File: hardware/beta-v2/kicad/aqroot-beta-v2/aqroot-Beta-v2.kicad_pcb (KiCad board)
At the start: 6 copper layers, 72 x 148 mm, 324 parts, among them J1 FH69-50S-0.5SH, J2 Molex_5025700893, J3 USB_C_Receptacle_USB2.0_16P, J4 JST-PH-2 BATTERY, J5 COMMUNITY_PORT_1x24, J6 JST-PH-2 SPEAKER, J7 BM02B-ACHSS-GAN-ETF, J8 QWIIC_STEMMA_QT, Q1 AO3400A, Q10 2N7002, Q2 NTMD4820N, Q3 NTMD4820N, Q4 BSS138, Q5 AO3401A, Q6 BSS138, Q7 BSS138, Q8 BSS138, Q9 BSS138, SW1 BOOT, SW2 UP, SW3 DOWN, SW4 LEFT, SW5 RIGHT, SW6 A_SELECT, SW7 B_BACK, SW9 SW_SPDT, U1 ESP32-S3-WROOM-1, U10 USBLC6-2SC6, U11 BQ25185, U12 TPS63020, U13 TPS61023, U14 MAX17048, U16 TCA4307DGKR, U17 TPS61169DCKR, U18 LTC4368-1, U19 TLV7032, U2 PCAL9535APW, U20 TPS22950C, U21 TPS61023, U22 TPS22950C, U23 PCAL9535APW, U3 PCAL9535APW, U4 BMI270, U5 MAX98357A, U6 TSOP38238, U7 E07-400M10S, U8 E22-900M22S, U9 ST25R3916-AQET, Y1 27.12MHz 10pF 3225-4P

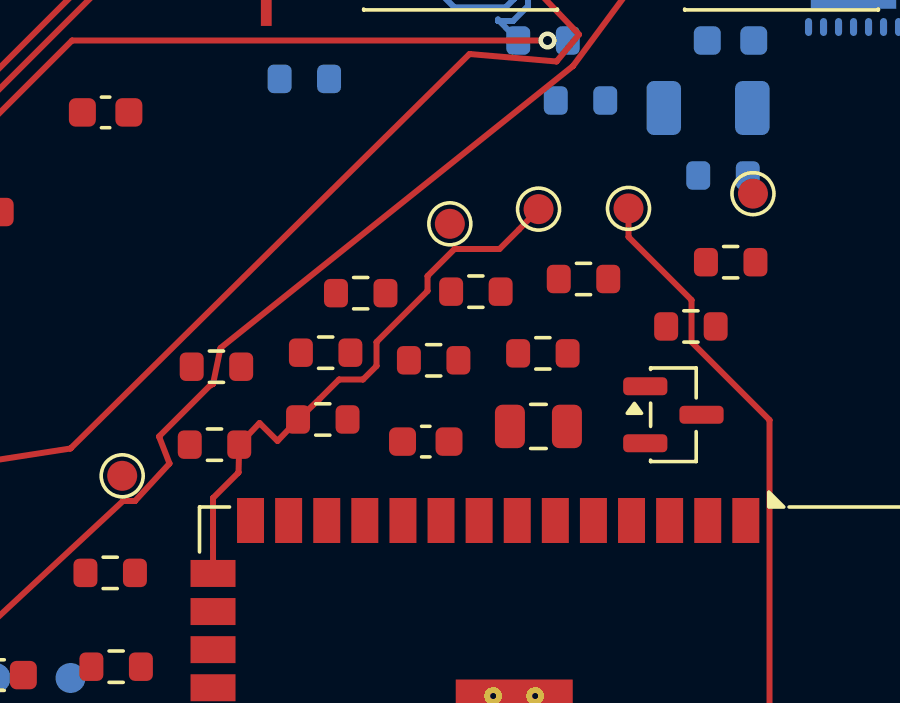
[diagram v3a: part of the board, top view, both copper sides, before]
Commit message: FBV2-P2-022: D-320 FIFTEENTH REST-OF-BOARD INCREMENTAL INCREMENT ROUTED + PROMOTED — the IR transmit carrier CONTROL leg IR_TX_GPIO16 (U1.9 ESP32 GPIO16 -> R22.1 series-drive resistor), a dedicated 2-pad point-to-point net, SAME-LAYER F.Cu MST with NO via (the cleanest class), a clean increment in an OPEN region 35.2 mm clear of BAT_PROTECTED_P (zero D-269 involvement); the low-current MCU control GPIO isolated by series R22 from the IR_GATE switch node + IR_LED_A/K emitter power (both excluded switching/emitter nets); a governed CTO ACCEPT + PROMOTE, ZERO router-logic change
Screen w/screen_020.py (142 unrouted rest nets, 42 ALLOW/100 EXCL; auto-classifier
converter-switching/USB-C traps rejected on role) + geometry vet w/vet_021.py verified
the isolation (/IR_TX_GPIO16 = {U1.9,R22.1}; R22.2 belongs to the separate IR_GATE net;
emitter power is IR_LED_A/K) and selected IR_TX_GPIO16 over Net-(U1-EN)/RESERVED_SPARE on
merit. GROUPS['IR_TX_GPIO16'] entry only; route ALL OK (13 F.Cu seg, 0 via, legal
same-layer detour around the GND pinch); gate PASS every check; promote.

sha 57dcc8af.. -> 4e706490389655cb8b68f8c15249a813072f36a9ea9e6ffaeb1fdd2194c0bf34;
tracks 716->729 (+13 F.Cu 0.200mm); vias 67 (unchanged); ratsnest 672->671; journal
109->110. New G32 + incremental_probe_020.py; router_regression ALL PASS G1-G32 twice;
probes _006..020 + phaseB PASS; live_fingerprint bumped; independent kicad-cli DRC
clearance 0; D-269/D-264/DRU board-swap A/B pre-existing/intrinsic flakes (not
regressions). 141/164 rest nets unrouted. Rollback: pre-D-320 sha 57dcc8af.. (committed
D-319, parent 8d27e3a).

Co-Authored-By: Claude Opus 4.8 (1M context) <noreply@anthropic.com>
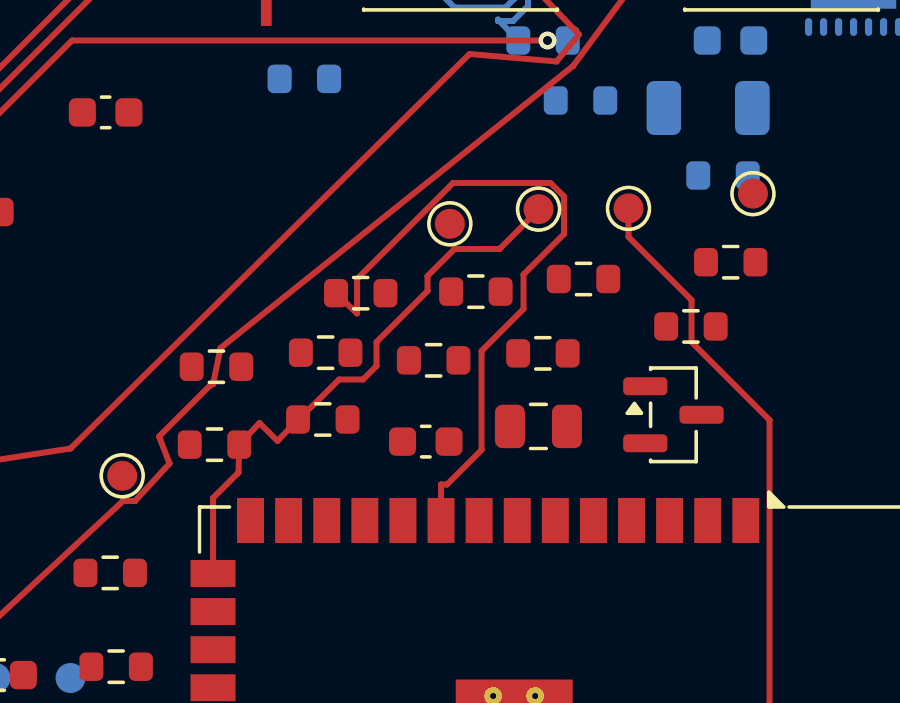
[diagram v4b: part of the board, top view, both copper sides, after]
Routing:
- net /IR_TX_GPIO16: track 0.00 -> 23.2 mm
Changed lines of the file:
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@@
+	)
+	(segment
+		(start 54.2 113.6)
+		(end 54.2 116.9)
+		(width 0.2)
+		(layer "F.Cu")
+		(net "/IR_TX_GPIO16")
+	)
+	(segment
+		(start 55.6 112.2)
+		(end 54.2 113.6)
+		(width 0.2)
+		(layer "F.Cu")
+		(net "/IR_TX_GPIO16")
+	)
+	(segment
+		(start 50.05 111.2)
+		(end 53.25 108)
+		(width 0.2)
+		(layer "F.Cu")
+		(net "/IR_TX_GPIO16")
+	)
+	(segment
+		(start 53.05 118.05)
+		(end 52.85 118.05)
+		(width 0.2)
+		(layer "F.Cu")
+		(net "/IR_TX_GPIO16")
+	)
+	(segment
+		(start 56.5 108)
+		(end 56.95 108.45)
+		(width 0.2)
+		(layer "F.Cu")
+		(net "/IR_TX_GPIO16")
+	)
+	(segment
+		(start 52.85 119.25)
+		(end 52.85 118.05)
+		(width 0.2)
+		(layer "F.Cu")
+		(net "/IR_TX_GPIO16")
+	)
+	(segment
+		(start 50.05 112.35)
+		(end 50.05 111.2)
+		(width 0.2)
+		(layer "F.Cu")
+		(net "/IR_TX_GPIO16")
+	)
+	(segment
+		(start 53.25 108)
+		(end 56.5 108)
+		(width 0.2)
+		(layer "F.Cu")
+		(net "/IR_TX_GPIO16")
+	)
+	(segment
+		(start 54.2 116.9)
+		(end 53.05 118.05)
+		(width 0.2)
+		(layer "F.Cu")
+		(net "/IR_TX_GPIO16")
+	)
+	(segment
+		(start 55.6 111.05)
+		(end 55.6 112.2)
+		(width 0.2)
+		(layer "F.Cu")
+		(net "/IR_TX_GPIO16")
+	)
+	(segment
+		(start 49.348174 111.672363)
+		(end 50.05 112.35)
+		(width 0.2)
+		(layer "F.Cu")
+		(net "/IR_TX_GPIO16")
+	)
+	(segment
+		(start 56.95 109.7)
+		(end 55.6 111.05)
+		(width 0.2)
+		(layer "F.Cu")
+		(net "/IR_TX_GPIO16")
+	)
+	(segment
+		(start 56.95 108.45)
+		(end 56.95 109.7)
+		(width 0.2)
+		(layer "F.Cu")
+		(net "/IR_TX_GPIO16")
 	)
 	(segment

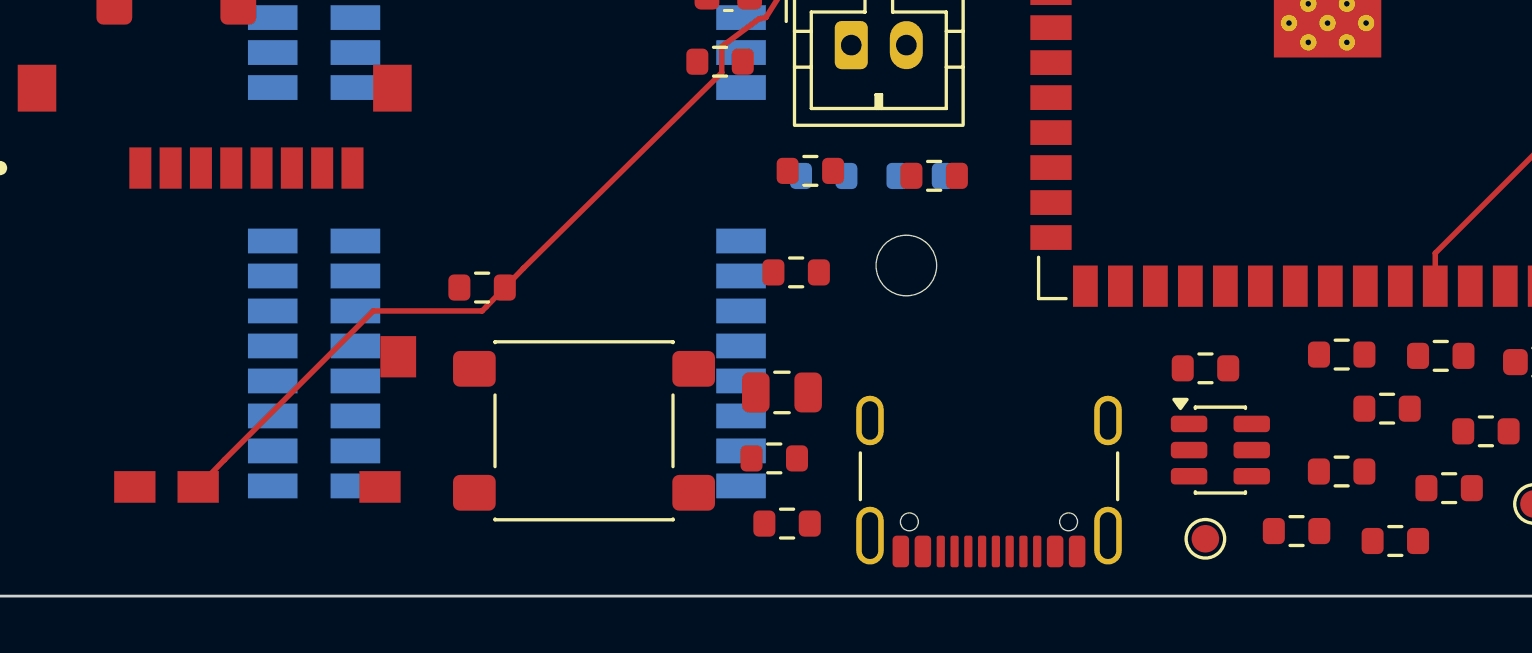
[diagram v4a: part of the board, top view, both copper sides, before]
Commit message: FBV2-P2-023: D-321 SIXTEENTH REST-OF-BOARD INCREMENTAL INCREMENT ROUTED + PROMOTED — the microSD SPI chip-select SD_CS_N (J2.2 socket / R25.2 / U1.25 MCU), a genuine functional POINT-TO-POINT control (NOT a shared SPI data/clock bus line), a 3-pad ALL-F.Cu SAME-LAYER MST with NO via (the cleanest class), a clean increment in an OPEN region 50.1 mm clear of BAT_PROTECTED_P (zero D-269 involvement); the mandate's headline candidate Net-(U1-EN) (group MCU_EN_RC, the ESP32 EN power-on-reset RC) was scratch-tested FIRST and hit a CHARACTERIZED LOCAL WALL (natural MST short edge C1.2<->U1.3 NO_PATH at 0.200 mm even on the 0.05/0.025 mm fine grid in the dense U1-EN pad pocket; the other edge only routes with a 58.46 mm detour 2.6x the straight — a poor path for a reset line also 0.335 mm from the USB_D_MCU_N diff pair), annotated do-NOT-naively-retry; SD_CS_N chosen over the RESERVED_SPARE spare per mandate; a governed CTO ACCEPT + PROMOTE, ZERO router-logic change
Starting HEAD bb7fed4 (D-320; pushed; origin/master identical; AUTH 4e706490..., 729/67, ratsnest 671, journal 110). Screen w/screen_020.py (141 unrouted, 41 ALLOW/100 EXCL; converter-switching/IR-emitter/USB-C auto-ALLOW traps rejected on role) + geometry vet w/vet_021.py (Net-(U1-EN) cong 66, RESERVED_SPARE cong 84, SD_CS_N cong 102). route ALL OK (J2.2<->U1.25 48.420 mm + U1.25<->R25.2 21.081 mm, 20 F.Cu seg, 0 via); gate PASS every check (0 Phase-A altered, 20 new items all target-net, 0 zones fill-changed — no via, open_edges 2->0, 0 prior pairs regressed, ratsnest 671->669 -2, no new/worse DRC, unconnected 499->499); promote re-ran gate PASS, AUTH sha undrifted, merged 2 REST_INC edges.

PROMOTED: sha256 4e706490... -> 68d44b54df91d607f689215c0da5db249b13fcd1ac189b9ab78ceb6366d25e46; tracks 729->749 (+20 F.Cu 0.200 mm); vias 67 (unchanged — no via); 6 layers / 41 zones; ratsnest 671->669 (-2); journal 110->112 (+2 REST_INC). Real KiCad DRC identical (solder_mask_bridge:1 + hole_clearance:5 + lib_footprint_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
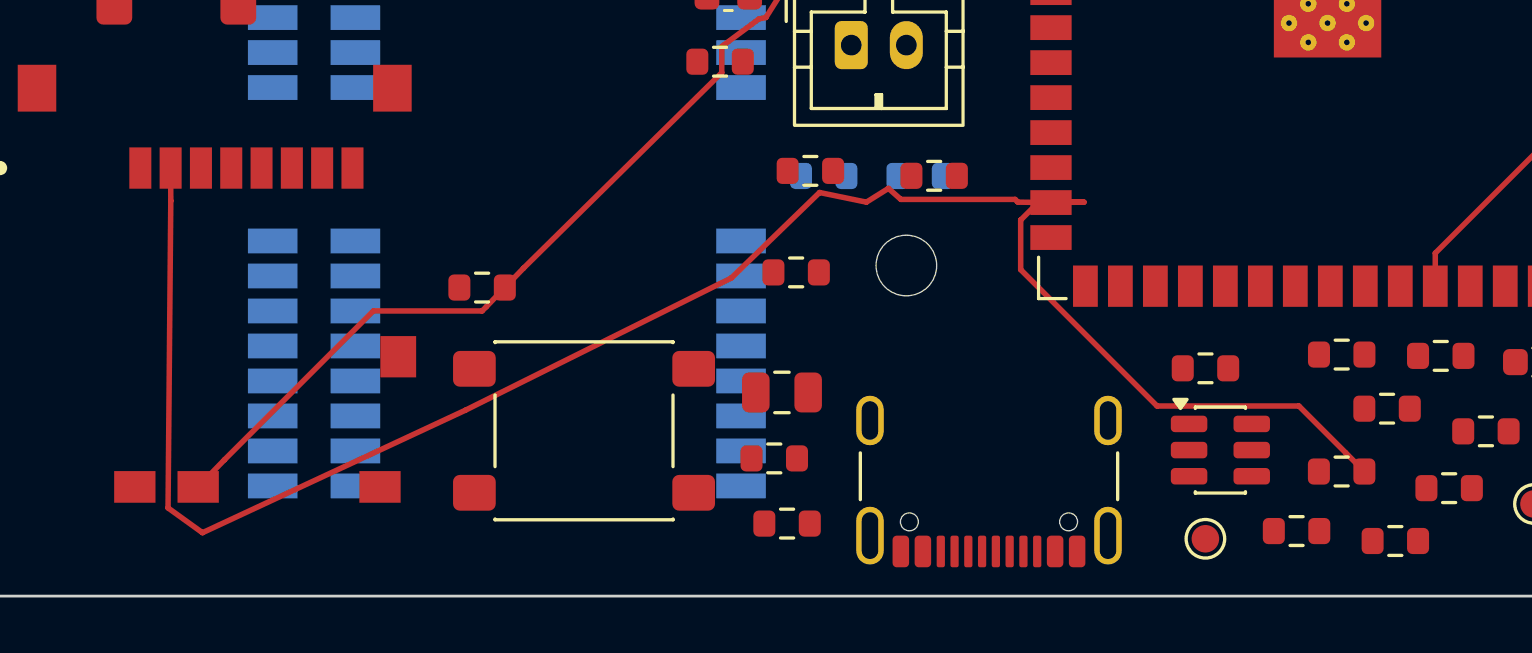
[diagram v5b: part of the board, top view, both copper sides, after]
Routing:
- net /SD_CS_N: track 0.00 -> 69.5 mm
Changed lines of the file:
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@@
+	)
+	(segment
+		(start 14.45 145.7)
+		(end 24 141.25)
+		(width 0.2)
+		(layer "F.Cu")
+		(net "/SD_CS_N")
+	)
+	(segment
+		(start 44.15 136.15)
+		(end 49.1 141.1)
+		(width 0.2)
+		(layer "F.Cu")
+		(net "/SD_CS_N")
+	)
+	(segment
+		(start 24 141.25)
+		(end 33.65 136.45)
+		(width 0.2)
+		(layer "F.Cu")
+		(net "/SD_CS_N")
+	)
+	(segment
+		(start 45.25 133.715)
+		(end 44.05 133.7)
+		(width 0.2)
+		(layer "F.Cu")
+		(net "/SD_CS_N")
+	)
+	(segment
+		(start 46.45 133.7)
+		(end 44.8 133.7)
+		(width 0.2)
+		(layer "F.Cu")
+		(net "/SD_CS_N")
+	)
+	(segment
+		(start 54.25 141.1)
+		(end 55.95 142.8)
+		(width 0.2)
+		(layer "F.Cu")
+		(net "/SD_CS_N")
+	)
+	(segment
+		(start 13.3 133.65)
+		(end 13.2 144.8)
+		(width 0.2)
+		(layer "F.Cu")
+		(net "/SD_CS_N")
+	)
+	(segment
+		(start 49.1 141.1)
+		(end 54.25 141.1)
+		(width 0.2)
+		(layer "F.Cu")
+		(net "/SD_CS_N")
+	)
+	(segment
+		(start 13.294 132.462)
+		(end 13.3 133.65)
+		(width 0.2)
+		(layer "F.Cu")
+		(net "/SD_CS_N")
+	)
+	(segment
+		(start 43.95 133.6)
+		(end 44.05 133.7)
+		(width 0.2)
+		(layer "F.Cu")
+		(net "/SD_CS_N")
+	)
+	(segment
+		(start 44.8 133.7)
+		(end 44.15 134.35)
+		(width 0.2)
+		(layer "F.Cu")
+		(net "/SD_CS_N")
+	)
+	(segment
+		(start 39.35 133.2)
+		(end 39.8 133.6)
+		(width 0.2)
+		(layer "F.Cu")
+		(net "/SD_CS_N")
+	)
+	(segment
+		(start 39.8 133.6)
+		(end 43.95 133.6)
+		(width 0.2)
+		(layer "F.Cu")
+		(net "/SD_CS_N")
+	)
+	(segment
+		(start 36.85 133.35)
+		(end 38.55 133.7)
+		(width 0.2)
+		(layer "F.Cu")
+		(net "/SD_CS_N")
+	)
+	(segment
+		(start 38.55 133.7)
+		(end 39.35 133.2)
+		(width 0.2)
+		(layer "F.Cu")
+		(net "/SD_CS_N")
+	)
+	(segment
+		(start 44.15 134.35)
+		(end 44.15 136.15)
+		(width 0.2)
+		(layer "F.Cu")
+		(net "/SD_CS_N")
+	)
+	(segment
+		(start 56.625767 143.477741)
+		(end 55.95 142.8)
+		(width 0.2)
+		(layer "F.Cu")
+		(net "/SD_CS_N")
+	)
+	(segment
+		(start 45.25 133.715)
+		(end 46.45 133.7)
+		(width 0.2)
+		(layer "F.Cu")
+		(net "/SD_CS_N")
+	)
+	(segment
+		(start 33.65 136.45)
+		(end 36.85 133.35)
+		(width 0.2)
+		(layer "F.Cu")
+		(net "/SD_CS_N")
+	)
+	(segment
+		(start 13.2 144.8)
+		(end 14.45 145.7)
+		(width 0.2)
+		(layer "F.Cu")
+		(net "/SD_CS_N")
 	)
 	(segment

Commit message: FBV2-P2-024: D-322 SEVENTEENTH REST-OF-BOARD INCREMENTAL INCREMENT ROUTED + PROMOTED — the reserved/spare community expander GPIO RESERVED_SPARE (R130.2 / TP41.1 test point / U23.7 PCAL expander), a 3-pad ALL-B.Cu SAME-LAYER MST with NO via (the cleanest class), a clean increment in an OPEN region 15.5 mm clear of BAT_PROTECTED_P (zero D-269 involvement); the held clean alternate, PROMOTED after the mandate's meaningful display-control candidates DISP_CS_N (display SPI chip-select U1.18/R26.2/J1.38) and DISP_DC (display data/command U1.22/J1.37) both hit a CHARACTERIZED J1 display-FPC-connector wall (long interior haul NO_PATH at 0.200 mm even on the 0.05/0.025 mm fine grid) and after BOOT_N (the meaningful non-J1 alternative, the ESP32 boot-mode strap) routed ALL OK but only via poor 2.5x detours (~110 mm of copper across the congested MCU interior for a boot-critical strap — not equally clean, sensitivity treated carefully); RESERVED_SPARE chosen when no meaningful candidate was equally clean per the mandate; a governed CTO ACCEPT + PROMOTE, ZERO router-logic change.
Route ALL OK (two B.Cu runs R130.2<->U23.7 4.434 mm + U23.7<->TP41.1 10.939 mm, 10 seg, 0 via). Gate PASS every check (real full-board D-286: 0 Phase-A altered, 10 new items all target-net, 0 zones fill-changed — no via, net open_edges 2->0, 0 prior pairs regressed, ratsnest 669->667 -2, no new/worse DRC, unconnected 499->499). Promoted sha256 68d44b54... -> a861e30e5760515288ef9a3fc0c21ea6d3e9c31409f9181dd66d56ed0628efd1; tracks 749->759 (+10 B.Cu 0.200 mm); vias 67 (unchanged); 6 layers / 41 zones; ratsnest 669->667 (-2); journal 112->114 (+2 REST_INC).

Tests: new G34; G18-G33 auto-generalise -> router_regression ALL PASS G1-G34 twice (deterministic); new incremental_probe_022.py PASS; _006..021 + phaseB_bringup_probe_005 (759/67/114; 25 routed rest nets, 139 unrouted) PASS; live_fingerprint bumped once; incremental_baseline_006.json left stale-by-design (reverted). Independent kicad-cli DRC cleara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
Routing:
- net /08_BUTTONS_EXPANDERS/RESERVED_SPARE: track 0.00 -> 15.4 mm
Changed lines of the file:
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@@
+	)
+	(segment
+		(start 54.1375 97.675)
+		(end 52.95 97.7)
+		(width 0.2)
+		(layer "B.Cu")
+		(net "/08_BUTTONS_EXPANDERS/RESERVED_SPARE")
+	)
+	(segment
+		(start 52.95 95.75)
+		(end 52.95 97.7)
+		(width 0.2)
+		(layer "B.Cu")
+		(net "/08_BUTTONS_EXPANDERS/RESERVED_SPARE")
+	)
+	(segment
+		(start 52.75 95.55)
+		(end 52.95 95.75)
+		(width 0.2)
+		(layer "B.Cu")
+		(net "/08_BUTTONS_EXPANDERS/RESERVED_SPARE")
+	)
+	(segment
+		(start 55.3 97.55)
+		(end 59 93.85)
+		(width 0.2)
+		(layer "B.Cu")
+		(net "/08_BUTTONS_EXPANDERS/RESERVED_SPARE")
+	)
+	(segment
+		(start 59 93.85)
+		(end 62.05 93.85)
+		(width 0.2)
+		(layer "B.Cu")
+		(net "/08_BUTTONS_EXPANDERS/RESERVED_SPARE")
+	)
+	(segment
+		(start 55.3 97.7)
+		(end 55.3 97.55)
+		(width 0.2)
+		(layer "B.Cu")
+		(net "/08_BUTTONS_EXPANDERS/RESERVED_SPARE")
+	)
+	(segment
+		(start 52.035594 94.830964)
+		(end 52.75 95.55)
+		(width 0.2)
+		(layer "B.Cu")
+		(net "/08_BUTTONS_EXPANDERS/RESERVED_SPARE")
+	)
+	(segment
+		(start 54.1375 97.675)
+		(end 55.3 97.7)
+		(width 0.2)
+		(layer "B.Cu")
+		(net "/08_BUTTONS_EXPANDERS/RESERVED_SPARE")
+	)
+	(segment
+		(start 62.05 93.85)
+		(end 62.35 94.15)
+		(width 0.2)
+		(layer "B.Cu")
+		(net "/08_BUTTONS_EXPANDERS/RESERVED_SPARE")
+	)
+	(segment
+		(start 63 93.5)
+		(end 62.35 94.15)
+		(width 0.2)
+		(layer "B.Cu")
+		(net "/08_BUTTONS_EXPANDERS/RESERVED_SPARE")
 	)
 	(segment
